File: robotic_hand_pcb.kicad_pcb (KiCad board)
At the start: 4 copper layers, 55 x 58.5 mm, 108 parts, among them J1 2171750001, J10 A5, J11 A6, J12 A7, J13 JST 1x5 Male, J14 JST 1x5 Male, J15 JST 1x5 Male, J16 JST 1x5 Male, J17 JST 1x5 Male, J2 TC2050-IDC, J4 UART, J5 WS2812B, J6 A1, J7 A2, J8 A3, J9 A4, SW1 SPST, U1 LMR51430, U10 ACS712xLCTR-05B, U11 ACS712xLCTR-05B, U12 ACS712xLCTR-05B, U13 ACS712xLCTR-05B, U14 ULN2003ADR, U15 ULN2003ADR, U16 ULN2003ADR, U17 ULN2003ADR, U18 ULN2003ADR, U2 ld39150dt33-r, U3 TXB0104QPWRQ1, U4 STM32F446RET, U5 VL53L4CD, U7 BNO085, U8 ADS114S08, U9 ACS712xLCTR-05B, Y1 8M, Y2 32k768

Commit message: Cleanup silkscreen
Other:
- board text added: "JU6"
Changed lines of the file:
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@@
 		(tags "Through hole pin header THT 1x06 2.54mm single row")
 		(property "Reference" "U6"
-			(at 0 2.75 180)
+			(at 0 2.75 0)
 			(layer "B.SilkS")
+			(hide yes)
 			(effects
 				(font
@@
 		(tags "Through hole pin header THT 1x05 2.54mm single row")
 		(property "Reference" "J15"
-			(at 0 3 90)
+			(at 0 2.46 180)
 			(layer "B.SilkS")
 			(effects
@@
 	)
 	(gr_text "SCL"
-		(at 137.75 83 45)
+		(at 137.75 83 60)
 		(layer "B.SilkS")
 		(effects
@@
 	)
 	(gr_text "GND"
-		(at 140.25 83 45)
+		(at 140.25 83 60)
 		(layer "B.SilkS")
 		(effects
@@
 	)
 	(gr_text "XSHUT"
-		(at 130.25 83 45)
+		(at 130.25 83 60)
 		(layer "B.SilkS")
 		(effects
@@
 	)
 	(gr_text "3V3"
-		(at 142.75 83 45)
+		(at 142.75 83 60)
 		(layer "B.SilkS")
 		(effects
@@
 		)
 	)
+	(gr_text "JU6"
+		(at 145.25 81.25 90)
+		(layer "B.SilkS")
+		(effects
+			(font
+				(size 1 1)
+				(thickness 0.15)
+			)
+			(justify mirror)
+		)
+	)
 	(gr_text "SDA"
-		(at 135.25 83 45)
+		(at 135.25 83 60)
 		(layer "B.SilkS")
 		(effects
@@
 	)
 	(gr_text "INT"
-		(at 132.75 83 45)
+		(at 132.75 83 60)
 		(layer "B.SilkS")
 		(effects

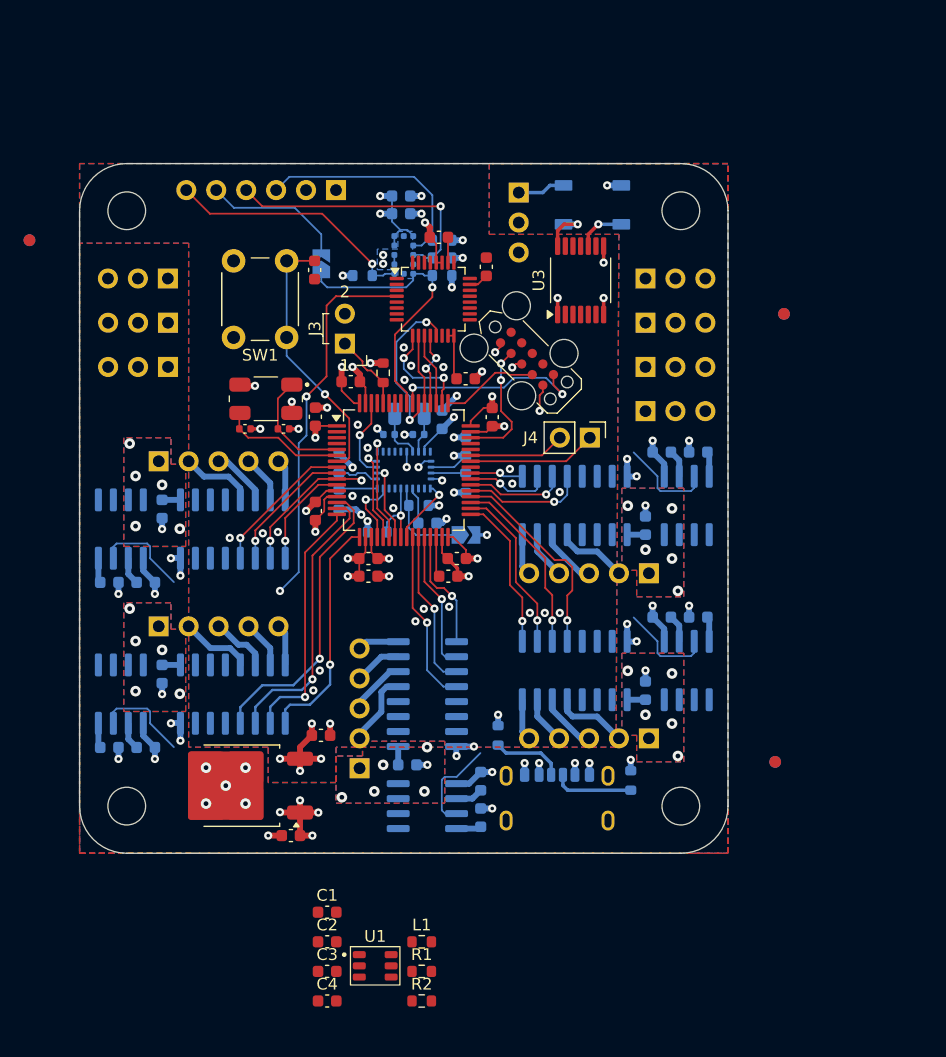
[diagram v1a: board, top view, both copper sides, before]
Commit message: Add WIP ADC routes
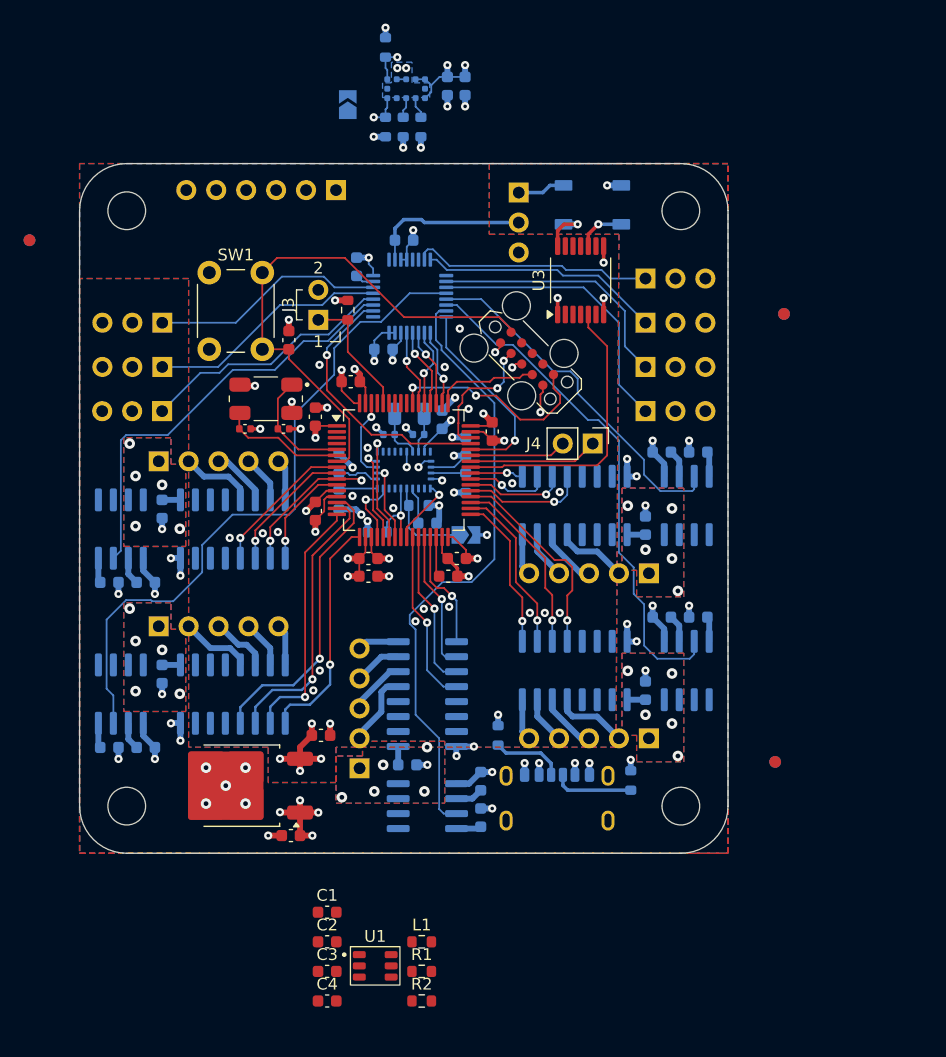
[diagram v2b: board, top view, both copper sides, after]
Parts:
- C25, C26, C27, U8: moved to B.Cu
- J10: renamed from J7; value A2 -> A5
- J11: renamed from J6; value A1 -> A6
- J6: renamed from J11; value A6 -> A1
- J7: renamed from J10; value A5 -> A2
- J8: renamed from J9; value A4 -> A3
- J9: renamed from J8; value A3 -> A4
- moved J12 41.0 mm to (128.0, 100.0), turned to 90 degrees
- moved J9 40.5 mm to (169.0, 88.8), turned to -90 degrees
- moved R8 19.4 mm to (146.9, 69.2), turned to -90 degrees
- moved U5 14.1 mm to (148.7, 72.7), turned to 90 degrees
- moved JP1 13.7 mm to (143.8, 74.0)
- moved R9 13.5 mm to (146.9, 75.9), turned to 90 degrees
- moved R6 11.6 mm to (148.4, 75.9), turned to 90 degrees
- moved C18 11.5 mm to (152.2, 72.4), turned to -90 degrees
- moved C27 11.0 mm to (144.5, 87.8)
- moved C19 10.8 mm to (153.7, 72.4), turned to -90 degrees
- moved R7 9.77 mm to (149.9, 75.9), turned to 90 degrees
- moved C26 7.41 mm to (146.8, 94.8)
- moved C14 6.34 mm to (138.8, 94.0), turned to -90 degrees
- moved R5 6.11 mm to (143.8, 91.4)
- moved J6 3.75 mm to (169.0, 100.0)
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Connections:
- J10 pad 1: /robotic_hand_pcb_analog/ADC7 -> /robotic_hand_pcb_analog/ADC10
- J11 pad 1: /robotic_hand_pcb_analog/ADC6 -> /robotic_hand_pcb_analog/ADC11
- J6 pad 1: /robotic_hand_pcb_analog/ADC11 -> /robotic_hand_pcb_analog/ADC6
- J7 pad 1: /robotic_hand_pcb_analog/ADC10 -> /robotic_hand_pcb_analog/ADC7
- J8 pad 1: /robotic_hand_pcb_analog/ADC9 -> /robotic_hand_pcb_analog/ADC8
- J9 pad 1: /robotic_hand_pcb_analog/ADC8 -> /robotic_hand_pcb_analog/ADC9
- U8 pad 19: /robotic_hand_pcb_analog/ADC12 -> /robotic_hand_pcb_analog/ADC1
- U8 pad 2: /robotic_hand_pcb_analog/ADC6 -> /robotic_hand_pcb_analog/ADC7
- U8 pad 20: /robotic_hand_pcb_analog/ADC11 -> /robotic_hand_pcb_analog/ADC12
- U8 pad 21: /robotic_hand_pcb_analog/ADC10 -> /robotic_hand_pcb_analog/ADC11
- U8 pad 22: /robotic_hand_pcb_analog/ADC9 -> /robotic_hand_pcb_analog/ADC10
- U8 pad 3: /robotic_hand_pcb_analog/ADC1 -> /robotic_hand_pcb_analog/ADC6
- U8 pad 31: /robotic_hand_pcb_analog/ADC8 -> /robotic_hand_pcb_analog/ADC9
- U8 pad 32: /robotic_hand_pcb_analog/ADC7 -> /robotic_hand_pcb_analog/ADC8
- U8 pad 5: /robotic_hand_pcb_analog/ADC3 -> /robotic_hand_pcb_analog/ADC5
- U8 pad 7: /robotic_hand_pcb_analog/ADC5 -> /robotic_hand_pcb_analog/ADC3
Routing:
- net /robotic_hand_pcb_analog/ADC3: track 8.17 -> 52.3 mm
- net /robotic_hand_pcb_analog/ADC4: track 8.17 -> 43.7 mm
- net /robotic_hand_pcb_analog/ADC1: track 8.17 -> 36.4 mm
- net /TIM1_CH1_PWM: track 0.00 -> 24.6 mm
- net /robotic_hand_pcb_analog/ADC6: track 0.00 -> 24.3 mm
- net /NRST: track 22.5 -> 45.7 mm, vias 1 -> 0
- net /GPIO_ADC_RST: track 0.00 -> 22.9 mm, vias 0 -> 1
- net /robotic_hand_pcb_analog/ADC5: track 8.17 -> 30.4 mm
- net /robotic_hand_pcb_analog/ADC12: track 0.00 -> 21.8 mm
- net /I2C1_SDA: track 23.5 -> 1.73 mm, vias 1 -> 0
- net /robotic_hand_pcb_analog/ADC7: track 0.00 -> 21.7 mm
- net /EXTI4_TOF_INT: track 23.8 -> 2.69 mm
- net /robotic_hand_pcb_analog/ADC9: track 0.00 -> 20.5 mm
- net /robotic_hand_pcb_analog/ADC11: track 0.00 -> 20.5 mm
- net /robotic_hand_pcb_analog/ADC8: track 0.00 -> 20.5 mm
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
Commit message: Add WIP ADC and TOF routing
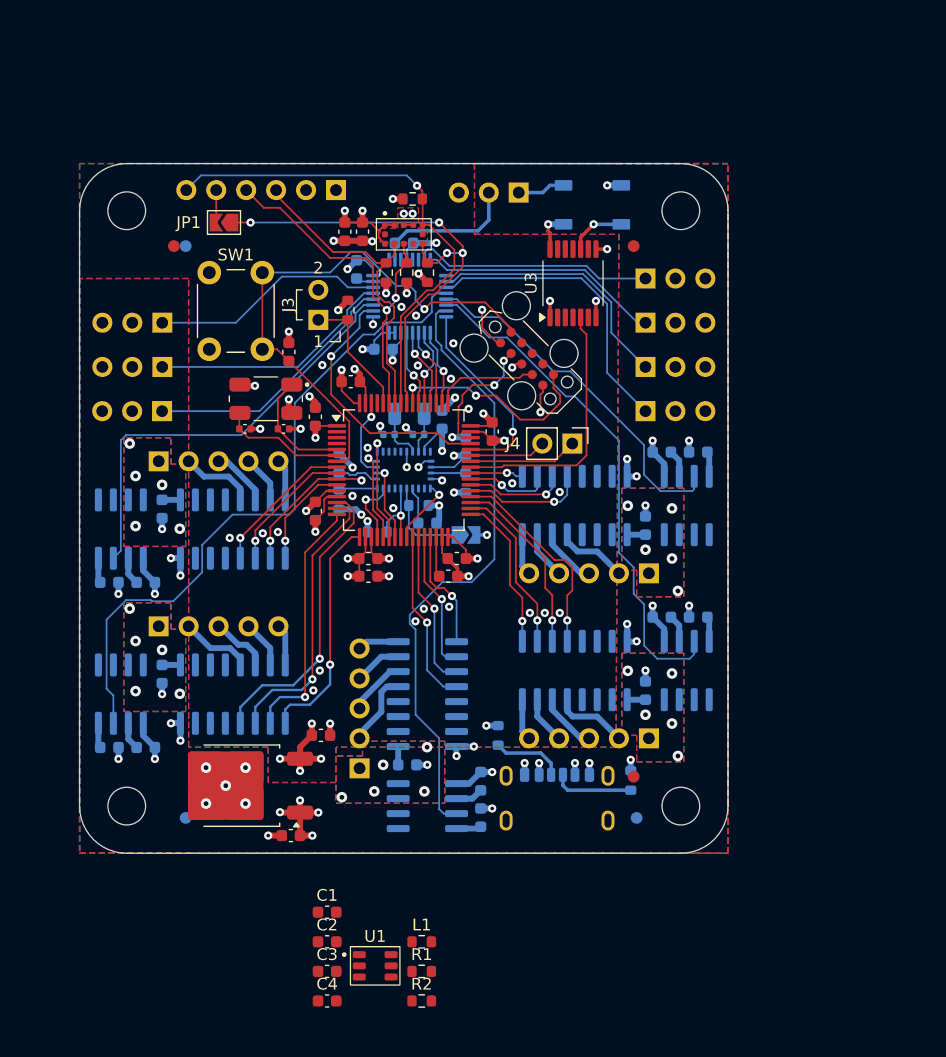
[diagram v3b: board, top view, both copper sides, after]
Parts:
- C18, C19, JP1, R6, R7, R8, R9, U5: moved to F.Cu
- moved FM4 51.1 mm to (130.0, 86.0)
- moved FM5 50.8 mm to (130.0, 134.5)
- moved C19 16.0 mm to (143.5, 84.8)
- moved JP1 14.5 mm to (133.2, 84.0), turned to 180 degrees
- moved C18 14.3 mm to (145.0, 84.8)
- moved FM2 14.0 mm to (168.0, 86.0)
- moved R8 13.1 mm to (149.2, 82.0), turned to 0 degrees
- moved R9 12.9 mm to (150.5, 88.2)
- moved R7 12.7 mm to (147.0, 88.2)
- moved FM6 12.7 mm to (168.2, 134.5)
- moved R6 12.4 mm to (148.8, 88.2)
- moved U5 12.4 mm to (148.5, 85.0)
- moved FM1 12.3 mm to (129.0, 86.0)
- moved FM3 12.1 mm to (168.0, 131.0)
- moved J4 1.74 mm to (162.8, 102.8)
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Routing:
- net /GPIO_TOF_XSHUT: track 2.94 -> 42.7 mm
- net /EXTI4_TOF_INT: track 2.69 -> 41.1 mm, vias 1 -> 4
- net /I2C1_SDA: track 1.73 -> 32.4 mm, vias 0 -> 2
- net /I2C1_SCL: track 1.81 -> 27.6 mm
- net GND: track 98.0 -> 102.2 mm, vias 87 -> 91
- net +3V3: track 64.3 -> 67.4 mm
- net Net-(JP1-B): track 0.00 -> 2.78 mm
- net /TIM1_CH1_PWM: track 24.6 -> 22.1 mm
- net +5V: track 37.9 -> 35.8 mm
- net /USART1_RX: track 8.22 -> 6.49 mm
- net /USART1_TX: track 11.0 -> 9.24 mm
- net /robotic_hand_pcb_analog/ADC6: track 24.3 -> 25.3 mm
- net /NRST: track 45.7 -> 46.4 mm, vias 0 -> 1
- net /TIM1_CH1_PWM_{5V}: track 4.15 -> 4.91 mm
- net unconnected-(U3-B1-Pad13): track 0.00 -> 0.55 mm
- added copper zone on F.Cu, net GND
- removed copper zone on B.Cu, net GND

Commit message: Add WIP buck converter layout
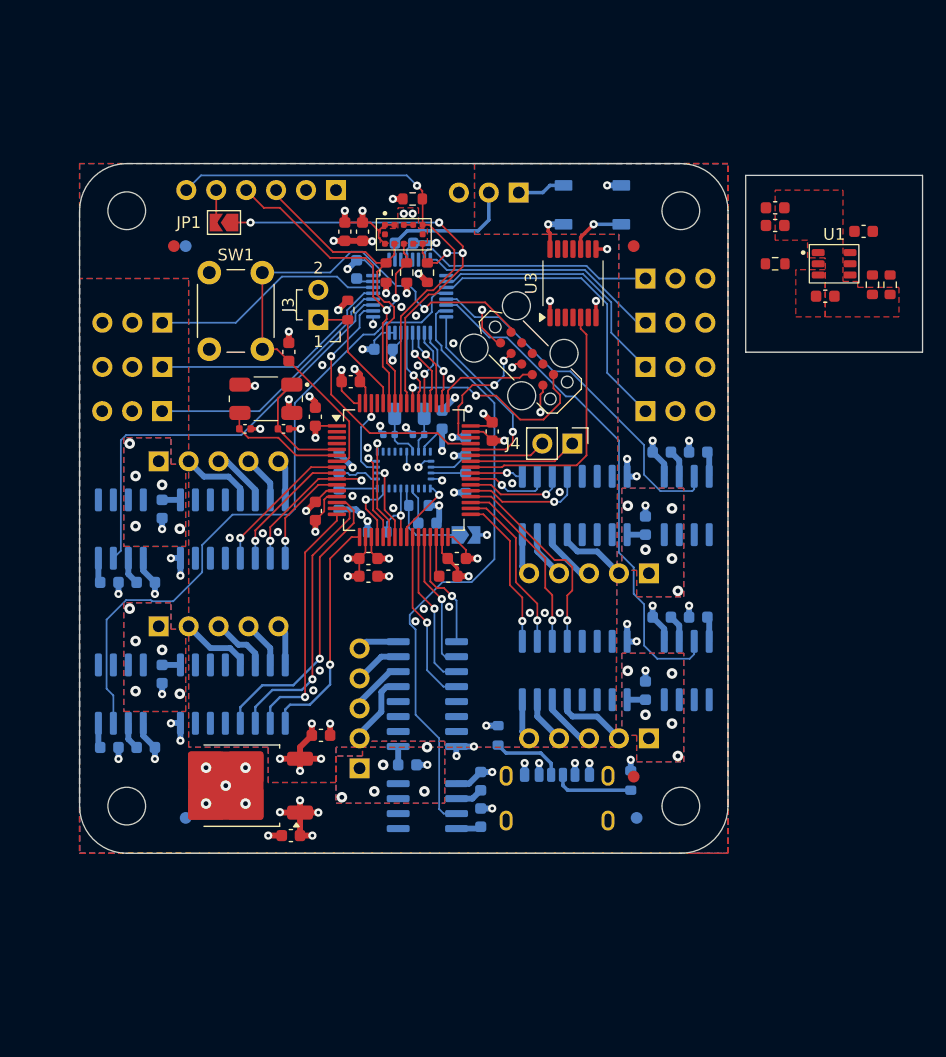
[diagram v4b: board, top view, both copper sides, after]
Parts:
- moved C4 76.0 mm to (180.0, 84.2), turned to 180 degrees
- moved C3 75.1 mm to (180.0, 82.8), turned to 180 degrees
- moved C1 73.5 mm to (187.5, 84.8), turned to 180 degrees
- moved R2 71.8 mm to (188.2, 89.3), turned to -90 degrees
- moved U1 71.1 mm to (185.0, 87.5)
- moved R1 70.5 mm to (189.8, 89.3), turned to -90 degrees
- moved C2 69.2 mm to (184.2, 90.2)
- moved L1 64.9 mm to (180.0, 87.5), turned to 180 degrees
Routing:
- added copper zone on F.Cu, net /V_{IN}
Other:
- board size 55 x 58.5 mm -> 71.5 x 58.5 mm

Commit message: Initial full PCB design, pass DRC
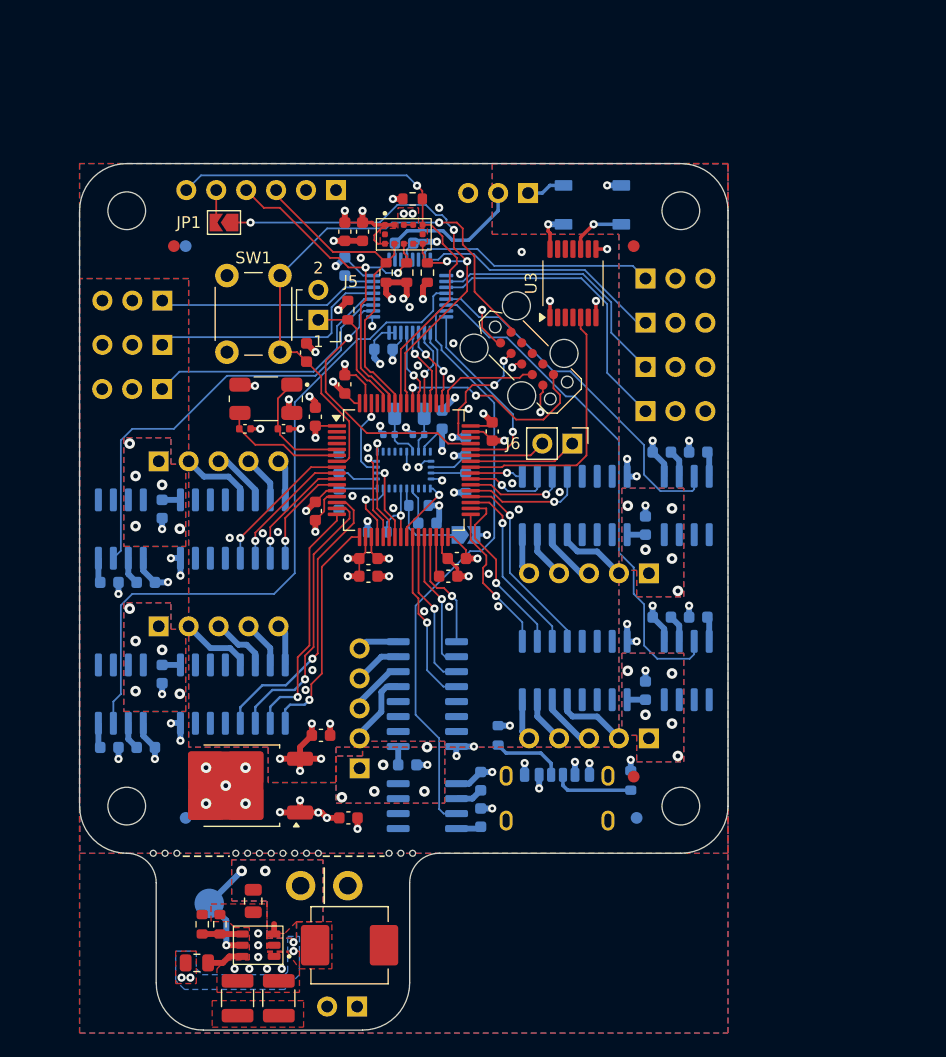
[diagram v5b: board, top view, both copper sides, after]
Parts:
- added ?: , , F.Cu at (141.2, 137.5)
- added ?: , , F.Cu at (148.2, 137.5)
- added ?: , , F.Cu at (129.2, 137.5)
- added ?: , , F.Cu at (134.2, 137.5)
- added ?: , , F.Cu at (135.2, 137.5)
- added ?: , , F.Cu at (147.2, 137.5)
- added ?: , , F.Cu at (138.2, 137.5)
- added ?: , , F.Cu at (140.2, 137.5)
- added ?: , , F.Cu at (149.2, 137.5)
- added ?: , , F.Cu at (136.2, 137.5)
- added ?: , , F.Cu at (139.2, 137.5)
- added ?: , , F.Cu at (127.2, 137.5)
- added ?: , , F.Cu at (128.2, 137.5)
- added ?: , , F.Cu at (137.2, 137.5)
- added J3: Battery, robotic_hand_pcb_connectors:battery, B.Cu at (141.8, 140.2)
- added J4: Battery, Connector_PinHeader_2.54mm:PinHeader_1x02_P2.54mm_Vertical, B.Cu at (144.5, 150.5)
- added TP1: TestPoint, TestPoint:TestPoint_Pad_D2.5mm, B.Cu at (132.0, 141.8)
- C1, C2: footprint Capacitor_SMD:C_0603_1608Metric -> Capacitor_SMD:C_0805_2012Metric
- C3, C4: footprint Capacitor_SMD:C_0603_1608Metric -> Capacitor_SMD:C_1210_3225Metric
- L1: footprint Resistor_SMD:R_0603_1608Metric -> robotic_hand_pcb_inductor:vishay_ihlp-2525cz
- moved C1 84.0 mm to (130.9, 146.8)
- moved C3 81.1 mm to (134.4, 149.8), turned to -90 degrees
- moved R1 79.7 mm to (131.4, 143.5), turned to 90 degrees
- moved C4 77.9 mm to (137.9, 149.8), turned to -90 degrees
- moved R2 77.5 mm to (132.9, 143.5), turned to 90 degrees
- moved U1 75.7 mm to (136.2, 145.3), turned to 180 degrees
- moved C2 70.6 mm to (135.7, 141.6), turned to -90 degrees
- moved L1 68.1 mm to (143.9, 145.3), turned to 0 degrees
- moved C5 5.10 mm to (143.8, 134.5), turned to 0 degrees
- moved J12 1.88 mm to (128.0, 90.6)
- moved J13 1.88 mm to (128.0, 94.4)
- moved J14 1.88 mm to (128.0, 98.1)
- moved SW1 1.52 mm to (133.5, 95.0)
- moved C14 1.50 mm to (140.2, 95.0)
- moved C27 1.03 mm to (143.5, 87.7)
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- renumbered J8 to J10, J9 to J11, J10 to J12, J11 to J13, J12 to J14, J13 to J15, J14 to J16, J15 to J17, J16 to J18, J17 to J19, J3 to J5, J4 to J6, J5 to J7, J6 to J8, J7 to J9
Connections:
- net /V_{IN} renamed +VSUPPLY
- net Net-(U1-SW) renamed /BUCK_SW
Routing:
- net +VSUPPLY: track 0.00 -> 10.2 mm, vias 0 -> 3
- net Net-(U1-FB): track 0.00 -> 3.40 mm
- net Net-(U1-CB): track 0.00 -> 3.13 mm
- net /M1_2: track 12.3 -> 9.98 mm, vias 2 -> 1
- net /EXTI4_TOF_INT: track 41.1 -> 42.9 mm
- net GND: track 102.2 -> 103.8 mm, vias 91 -> 98
- net /robotic_hand_pcb_analog/ADC2: track 56.7 -> 58.0 mm
- net /robotic_hand_pcb_analog/ADC3: track 52.3 -> 51.0 mm
- net /robotic_hand_pcb_analog/ADC10: track 19.9 -> 18.7 mm
- net Net-(U8-REFOUT): track 1.50 -> 2.61 mm
- net /NRST: track 46.4 -> 47.5 mm
- net /M5_4: track 17.6 -> 16.7 mm
- net /I2C1_SDA: track 32.4 -> 31.5 mm
- net /M5_2: track 14.4 -> 15.2 mm
- net Net-(D1-DOUT): track 4.05 -> 3.28 mm
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- added copper zone on B.Cu, net +VSUPPLY
- added copper zone on B.Cu, net /BUCK_SW
- added copper zone on F.Cu, net /BUCK_SW
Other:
- board size 71.5 x 58.5 mm -> 55 x 73.5 mm
- board text added: "5V"
- board text added: "BAT+"
- board text added: "EN"
